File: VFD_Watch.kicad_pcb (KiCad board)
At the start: 2 copper layers, 67.8 x 55 mm, 65 parts, among them J1 USB_B_Micro, J2 I2C_Con, Q1 MBT3904DW1, SW1 B1, SW2 B2, SW3 B_RES, SW4 B_0, U1 MIC5219-3.3YM5, U10 IVL2-7_5, U2 DRV8837C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

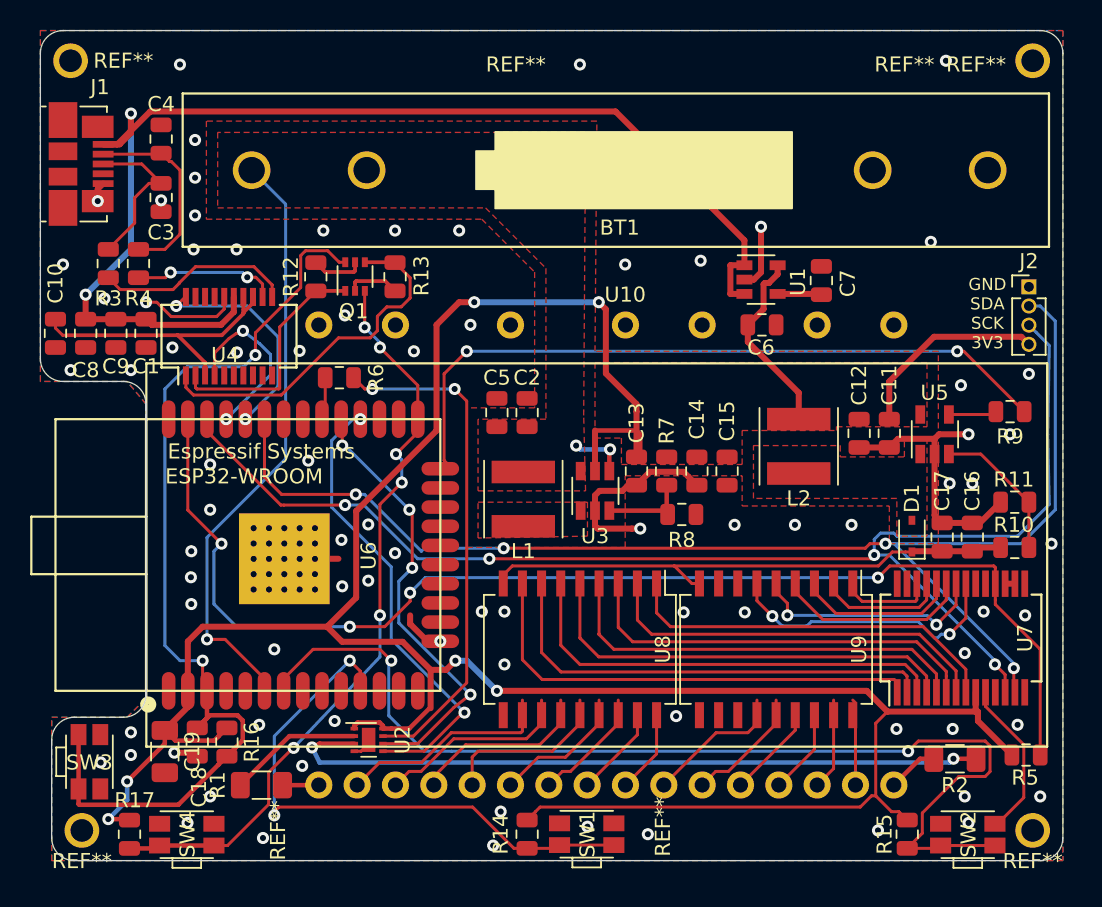
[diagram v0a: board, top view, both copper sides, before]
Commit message: fixed BAT INPUT to allow for LiPo voltages without damaging the ESP32, cleaned up silkscreen, updated graphics
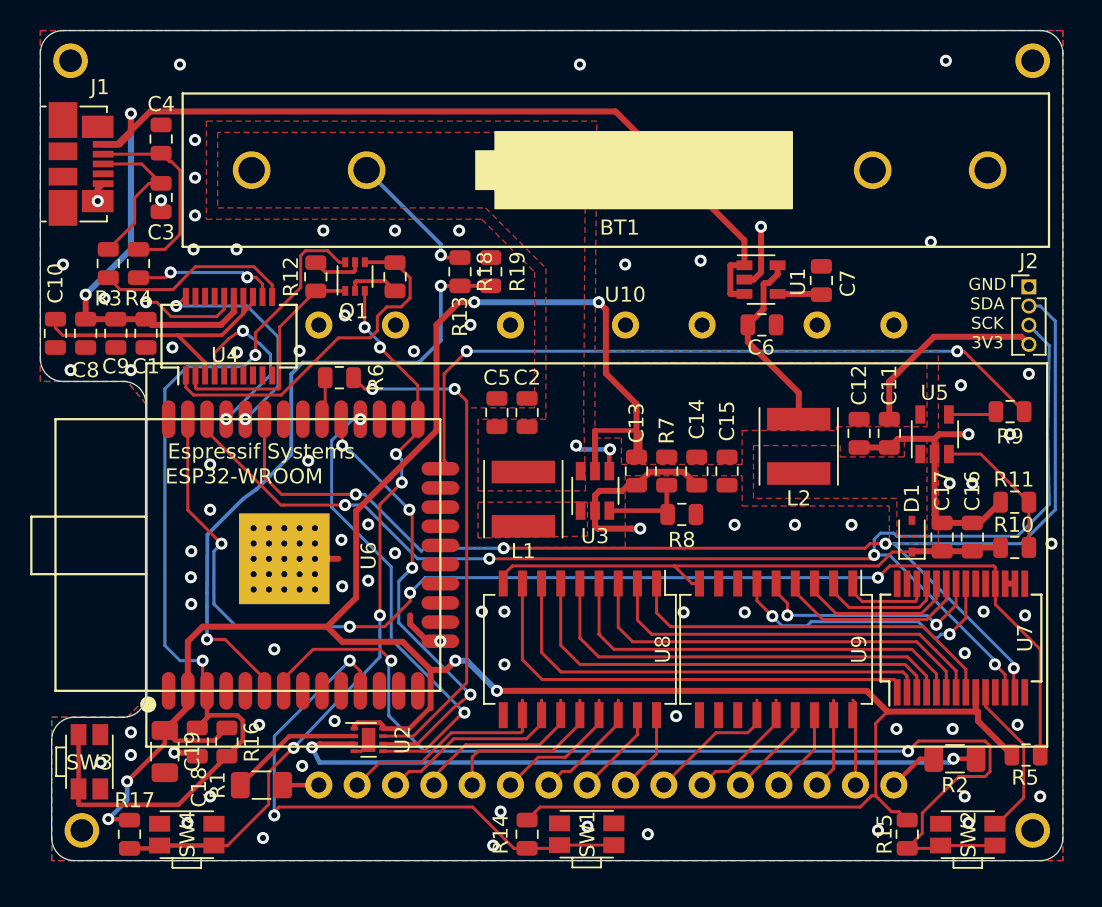
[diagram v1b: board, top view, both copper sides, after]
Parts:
- added R18: 10k, Resistor_SMD:R_0805_2012Metric, F.Cu at (114.6, 89.0)
- added R19: 10k, Resistor_SMD:R_0805_2012Metric, F.Cu at (116.6, 89.0)
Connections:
- U6 pad 6: +BATT -> Net-(R18-Pad2)
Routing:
- net Net-(R18-Pad2): track 0.00 -> 43.4 mm, vias 0 -> 2
- net +BATT: track 43.7 -> 12.8 mm
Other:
- board text added: "Pakue (2019)"
- board text added: "V1.1"
- board text removed: "Pakue (2018)"
- board text removed: "V1.0"
